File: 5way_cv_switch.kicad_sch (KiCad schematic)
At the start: 19 parts, among them J1 I/O connector, J2 5-way Switch Connector, U1 HT7550-1, U2 LMV321IDBVR

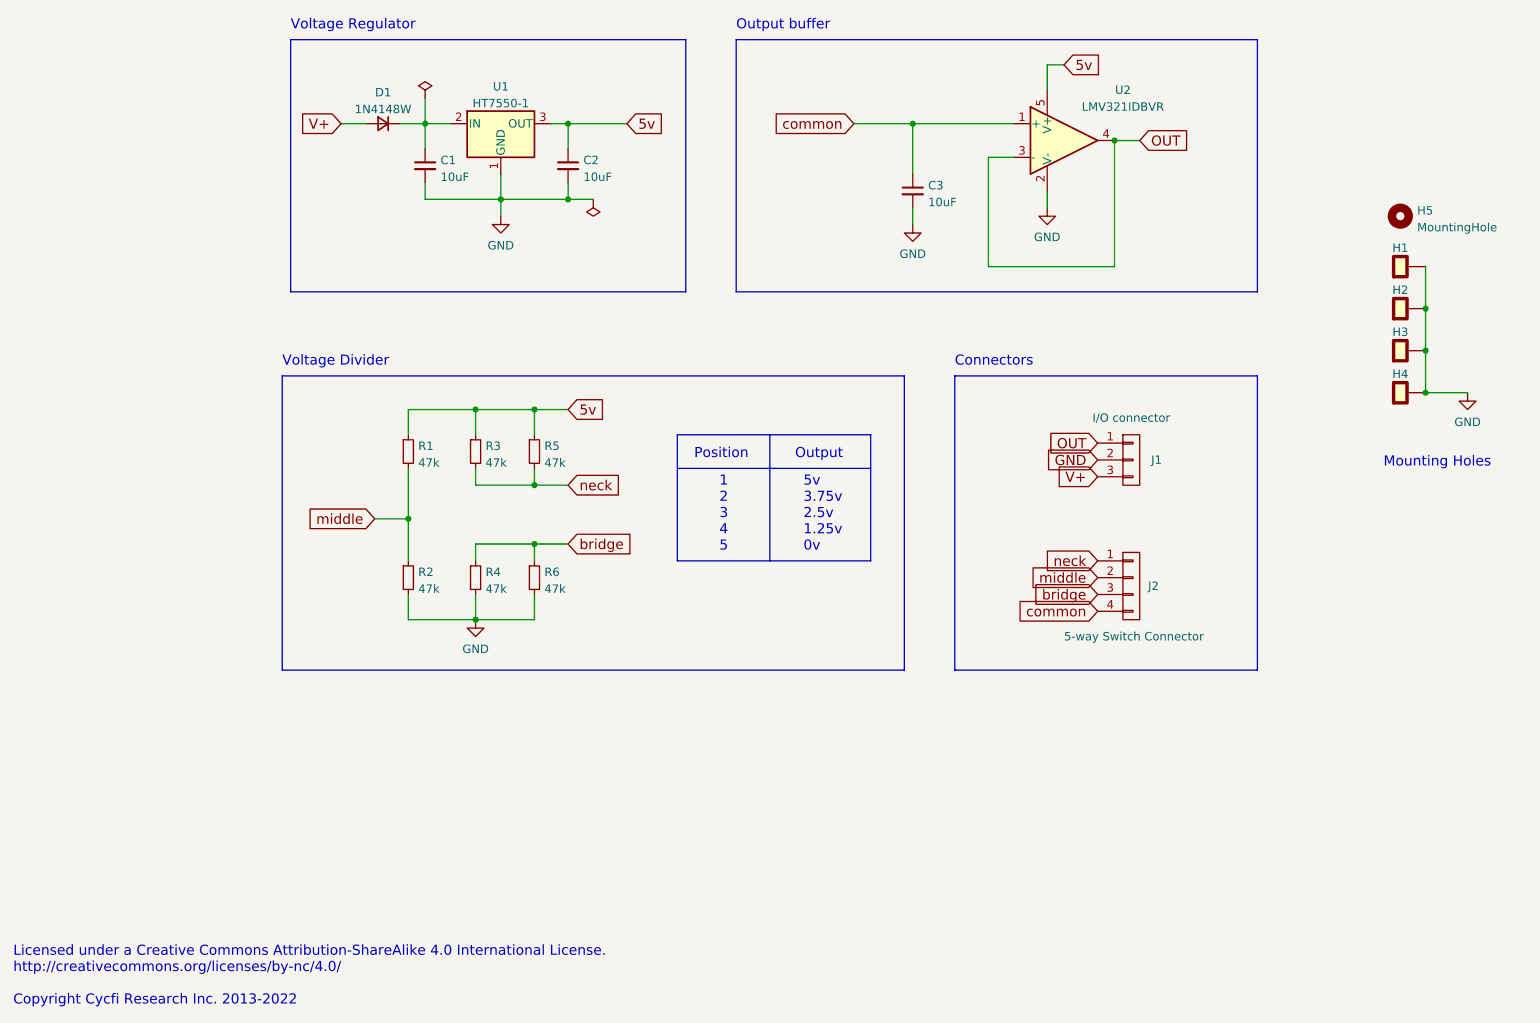
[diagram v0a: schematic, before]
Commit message: Update to KiCad 9
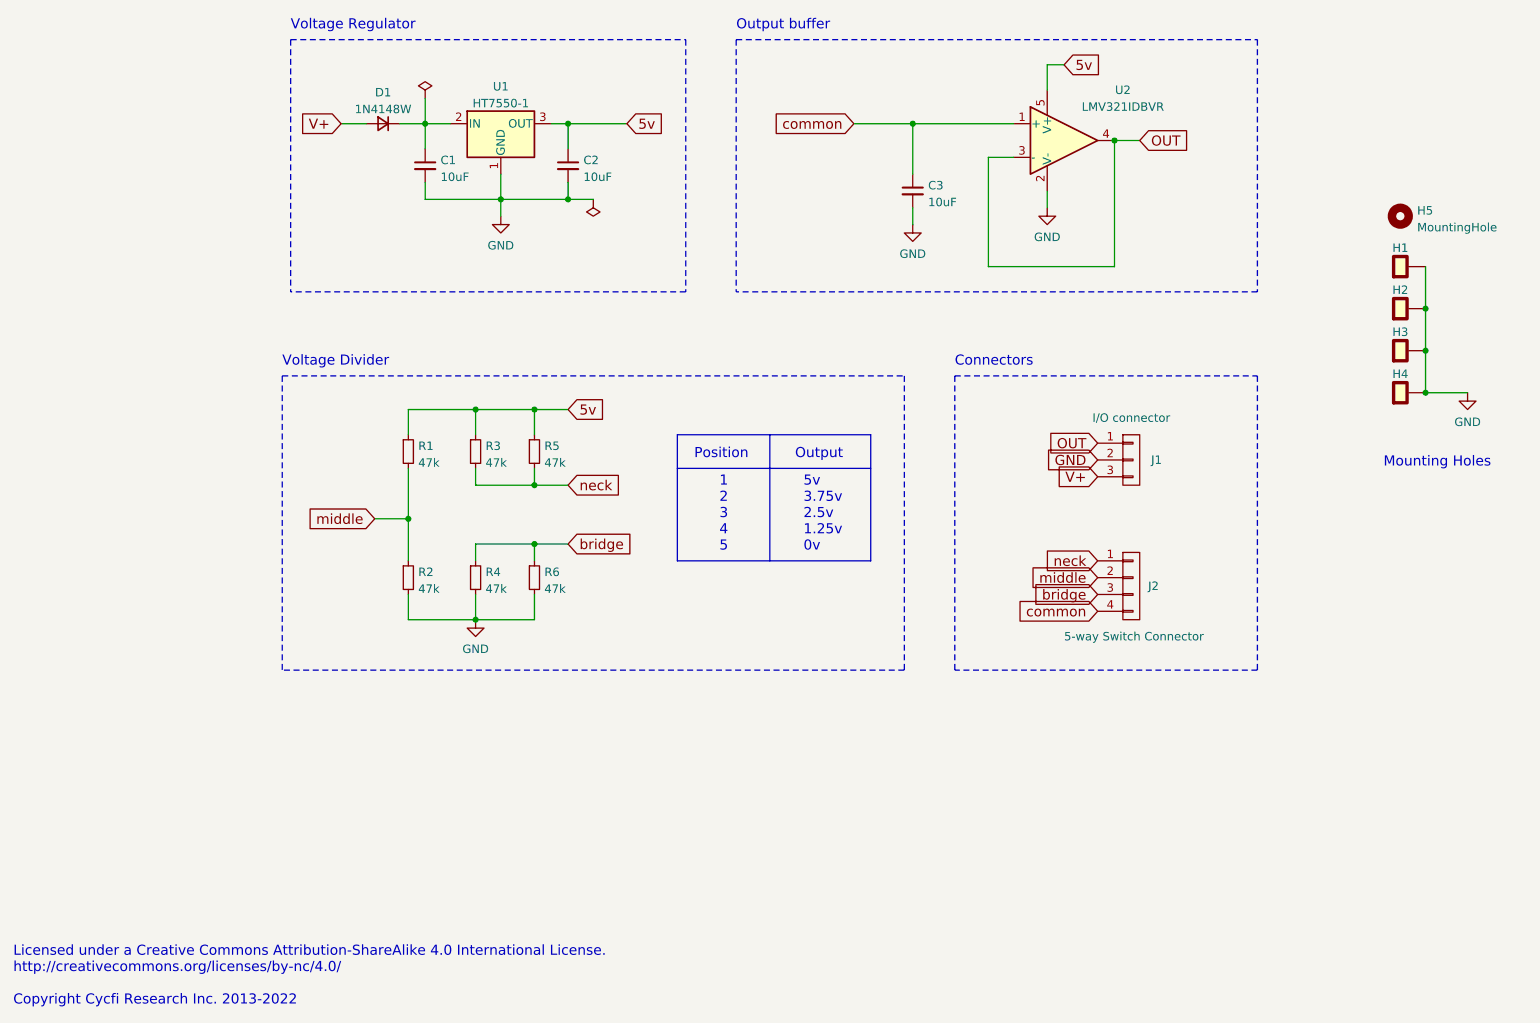
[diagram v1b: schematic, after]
